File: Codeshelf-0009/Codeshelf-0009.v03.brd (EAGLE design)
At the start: 55.8 x 40.9 mm, 24 parts, among them U1 MC9S08QG-DT, U2 LED5060A, U3 RS485SOIC, U4 CAT9552

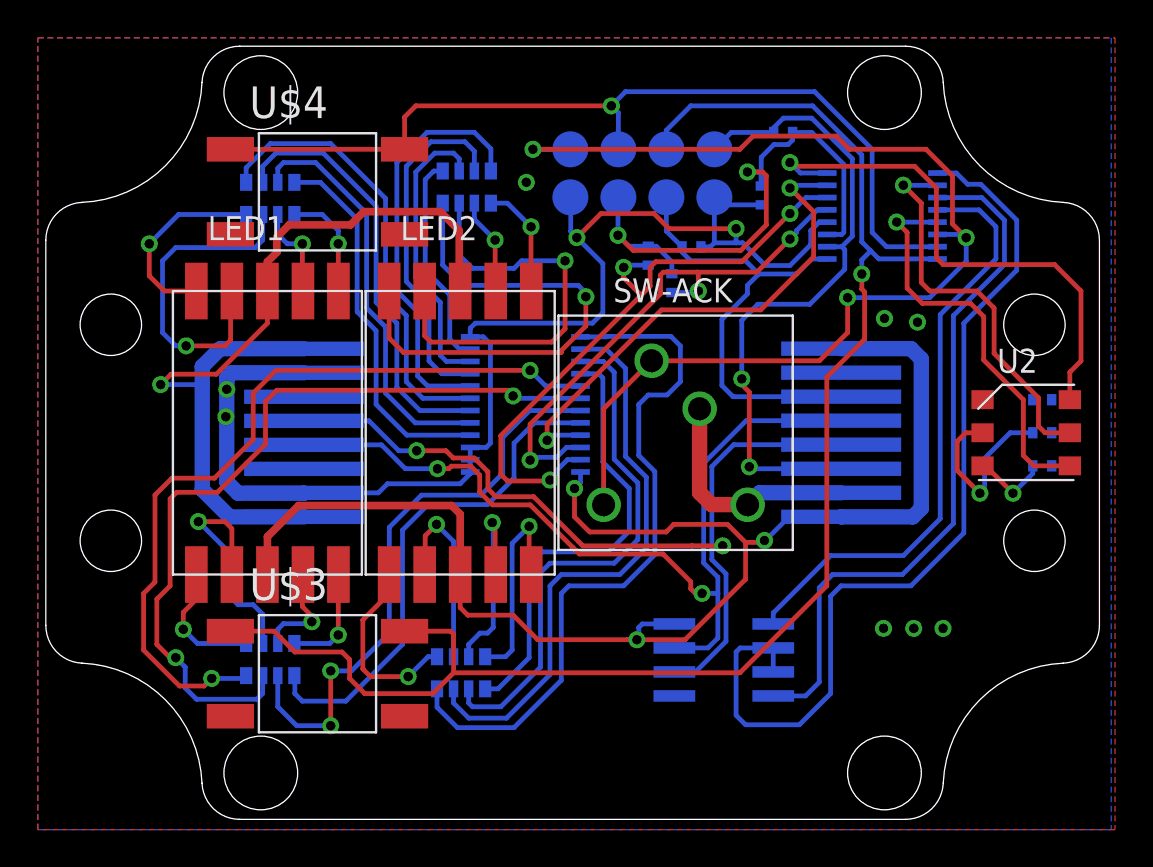
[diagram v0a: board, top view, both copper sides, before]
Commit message: Switched LED
Exchanged for WS2812 and reroute to match old PosCon pin assigments for
firmware compatibility.
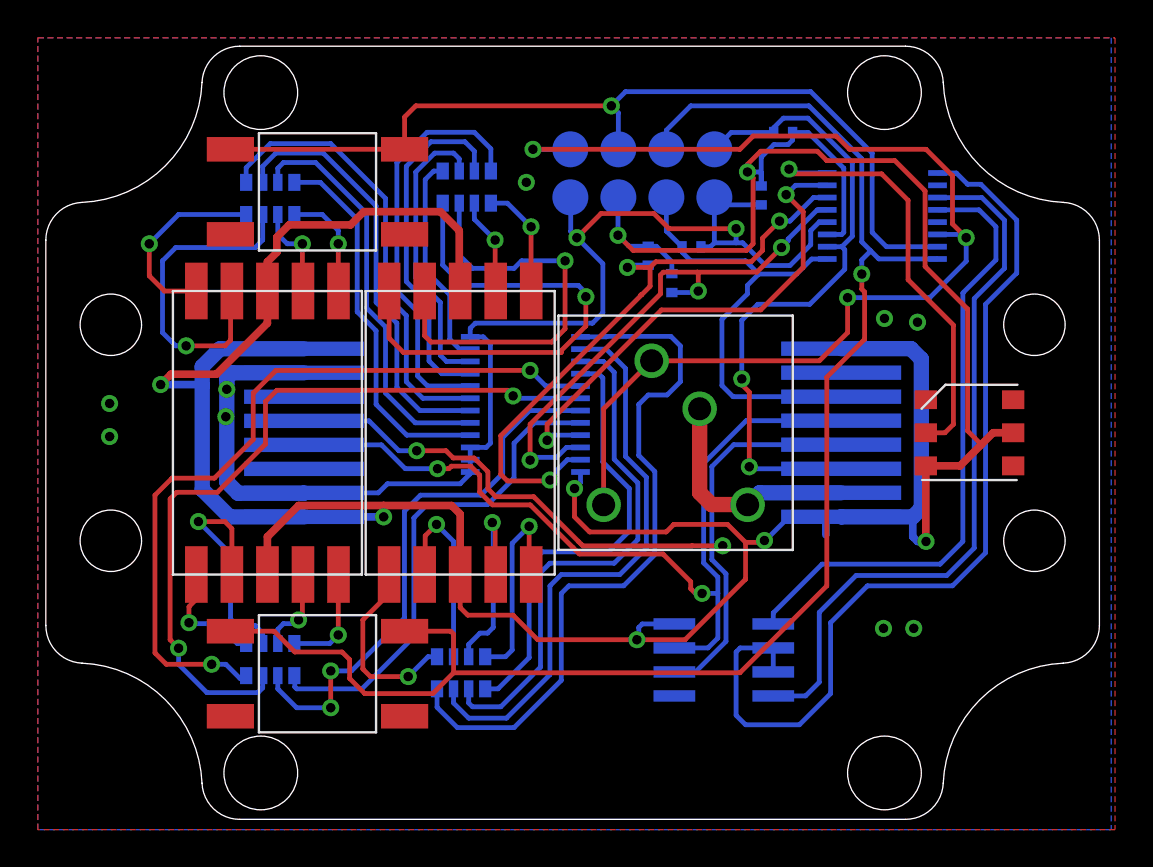
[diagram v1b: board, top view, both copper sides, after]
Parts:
- removed R2, R3, R4: 3.3K, GW-devices:RF-R0402
- removed U2: LED5060A, GW-devices:PLCC-6
- added U$2: WS2812, GW-devices:PLCC-6
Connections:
- removed net N$1: R2.1, U2.3
- removed net N$4: R4.1, U2.1
- removed net N$5: U1.13, U2.4
- removed net N$6: U1.10, U2.5
- removed net N$7: U1.8, U2.6
- net +3V3: now also U$2.3, U$2.5
- net GND: now also U$2.6; no longer R2.2, R3.2, R4.2
- net N$3: now also U$2.2, U1.8; no longer R3.1, U2.2
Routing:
- net +3V3: track 152.6 -> 194.2 mm, vias 6 -> 8
- net N$7: track 28.6 -> 0.00 mm, vias 1 -> 0
- net N$5: track 21.5 -> 0.00 mm, vias 1 -> 0
- net N$6: track 20.8 -> 0.00 mm, vias 1 -> 0
- net N$3: track 9.84 -> 23.6 mm
- net N$1: track 4.10 -> 0.00 mm, vias 1 -> 0
- net N$37: track 31.1 -> 29.2 mm
- net N$36: track 42.1 -> 40.4 mm
- net RX: track 31.6 -> 33.0 mm
- net N$35: track 41.9 -> 40.8 mm
- net N$39: track 5.44 -> 4.55 mm
- net TX: track 37.4 -> 38.1 mm
- net N$41: track 6.82 -> 6.19 mm
- net N$38: track 27.0 -> 26.4 mm
- net GND: vias 10 -> 11

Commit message: Completed new PosCon
Added BOM (csv and excel) and prepared bottom silkscreen.
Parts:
- SW-ACK: value SWITCH-TACTILE-320.03E11 -> SWITCH-TACTILE-320.01E11WHT; device GW-devices:SWITCH-TACTILE-320.03E11 -> GW-devices:SWITCH-TACTILE-320.01E11WHT
- U4: value CAT9552 -> PCA9552
- renumbered U$1 to J1-PROG, U$2 to U$5, U$2-PROG to J2
